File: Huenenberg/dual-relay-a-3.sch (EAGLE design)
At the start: 38 parts, among them J1 12V, J10 REV, J11 NORM, J12 REV, J13 NORM, J14 REV, J15 NORM, J16 REV, J17 NORM, J18 CTRL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

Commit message: Finishes routing of the turnout relay board.
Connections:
- removed net JN4: J5.1, J6.1, J7.1, J8.1
- net GND: now also J5.1, J6.1, J7.1, J8.1
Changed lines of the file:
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@@
 <junction x="66.04" y="121.92"/>
+</segment>
+<segment>
+<pinref part="J5" gate="G$1" pin="1"/>
+<wire x1="5.08" y1="71.12" x2="12.7" y2="71.12" width="0.1524" layer="91"/>
+<pinref part="GND2" gate="1" pin="GND"/>
+<pinref part="J8" gate="G$1" pin="1"/>
+<wire x1="12.7" y1="71.12" x2="12.7" y2="63.5" width="0.1524" layer="91"/>
+<wire x1="12.7" y1="63.5" x2="12.7" y2="55.88" width="0.1524" layer="91"/>
+<wire x1="12.7" y1="55.88" x2="12.7" y2="48.26" width="0.1524" layer="91"/>
+<wire x1="12.7" y1="48.26" x2="12.7" y2="43.18" width="0.1524" layer="91"/>
+<wire x1="5.08" y1="48.26" x2="12.7" y2="48.26" width="0.1524" layer="91"/>
+<junction x="12.7" y="48.26"/>
+<pinref part="J7" gate="G$1" pin="1"/>
+<wire x1="5.08" y1="55.88" x2="12.7" y2="55.88" width="0.1524" layer="91"/>
+<junction x="12.7" y="55.88"/>
+<pinref part="J6" gate="G$1" pin="1"/>
+<wire x1="5.08" y1="63.5" x2="12.7" y2="63.5" width="0.1524" layer="91"/>
+<junction x="12.7" y="63.5"/>
 </segment>
 </net>
@@
 </segment>
 </net>
-<net name="JN4" class="0">
-<segment>
-<pinref part="J5" gate="G$1" pin="1"/>
-<wire x1="5.08" y1="71.12" x2="12.7" y2="71.12" width="0.1524" layer="91"/>
-<pinref part="GND2" gate="1" pin="GND"/>
-<wire x1="12.7" y1="71.12" x2="12.7" y2="63.5" width="0.1524" layer="91"/>
-<pinref part="J8" gate="G$1" pin="1"/>
-<wire x1="12.7" y1="63.5" x2="12.7" y2="55.88" width="0.1524" layer="91"/>
-<wire x1="12.7" y1="55.88" x2="12.7" y2="48.26" width="0.1524" layer="91"/>
-<wire x1="12.7" y1="48.26" x2="12.7" y2="43.18" width="0.1524" layer="91"/>
-<wire x1="5.08" y1="48.26" x2="12.7" y2="48.26" width="0.1524" layer="91"/>
-<junction x="12.7" y="48.26"/>
-<pinref part="J7" gate="G$1" pin="1"/>
-<wire x1="5.08" y1="55.88" x2="12.7" y2="55.88" width="0.1524" layer="91"/>
-<junction x="12.7" y="55.88"/>
-<pinref part="J6" gate="G$1" pin="1"/>
-<wire x1="5.08" y1="63.5" x2="12.7" y2="63.5" width="0.1524" layer="91"/>
-<junction x="12.7" y="63.5"/>
-</segment>
-</net>

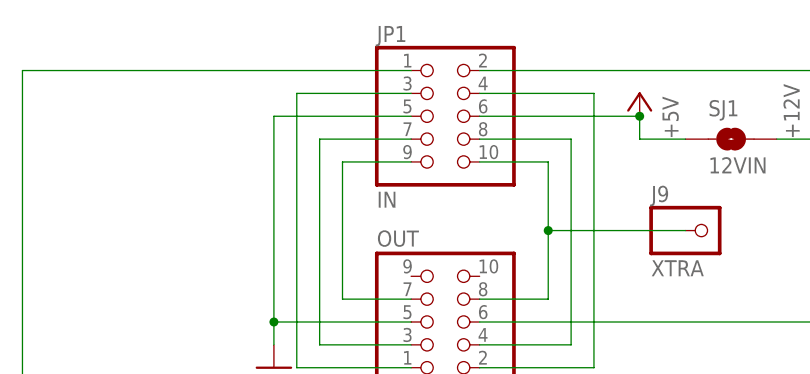
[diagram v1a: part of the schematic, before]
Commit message: Adds some labels to make the IN/OUT more understandable. Renames some nets for the labels.
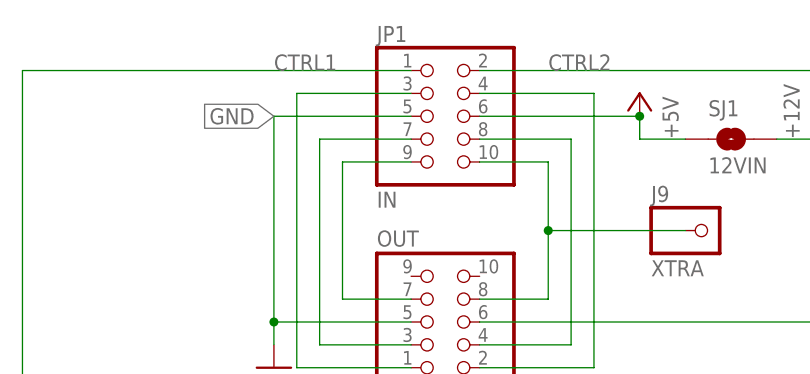
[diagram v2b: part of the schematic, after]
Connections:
- net N$18 renamed CTRL2
- net N$2 renamed CTRL1
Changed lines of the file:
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@@
 <wire x1="66.04" y1="144.78" x2="66.04" y2="121.92" width="0.1524" layer="91"/>
 <junction x="66.04" y="121.92"/>
+<label x="66.04" y="144.78" size="1.778" layer="95" rot="R180" xref="yes"/>
 </segment>
 <segment>
@@
 </segment>
 </net>
-<net name="N$2" class="0">
+<net name="CTRL1" class="0">
 <segment>
 <pinref part="R1" gate="G$1" pin="1"/>
@@
 <wire x1="38.1" y1="149.86" x2="38.1" y2="58.42" width="0.1524" layer="91"/>
 <junction x="38.1" y="58.42"/>
+<label x="66.04" y="149.86" size="1.778" layer="95"/>
 </segment>
 </net>
@@
 </segment>
 </net>
-<net name="N$18" class="0">
+<net name="CTRL2" class="0">
 <segment>
 <pinref part="JP1" gate="A" pin="2"/>
@@
 <junction x="129.54" y="53.34"/>
 <junction x="129.54" y="58.42"/>
+<label x="96.52" y="149.86" size="1.778" layer="95"/>
 </segment>
 </net>
